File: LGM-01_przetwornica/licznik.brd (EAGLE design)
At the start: 68 x 48 mm, 34 parts, among them IC1 NE555, J1 22-27-2041-04, Q1 BC557, Q2 BC557, Q3 BC557, Q4 BC557, Q5 BC557, Q6 BC557, Q7 IRF840, T1 BC547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

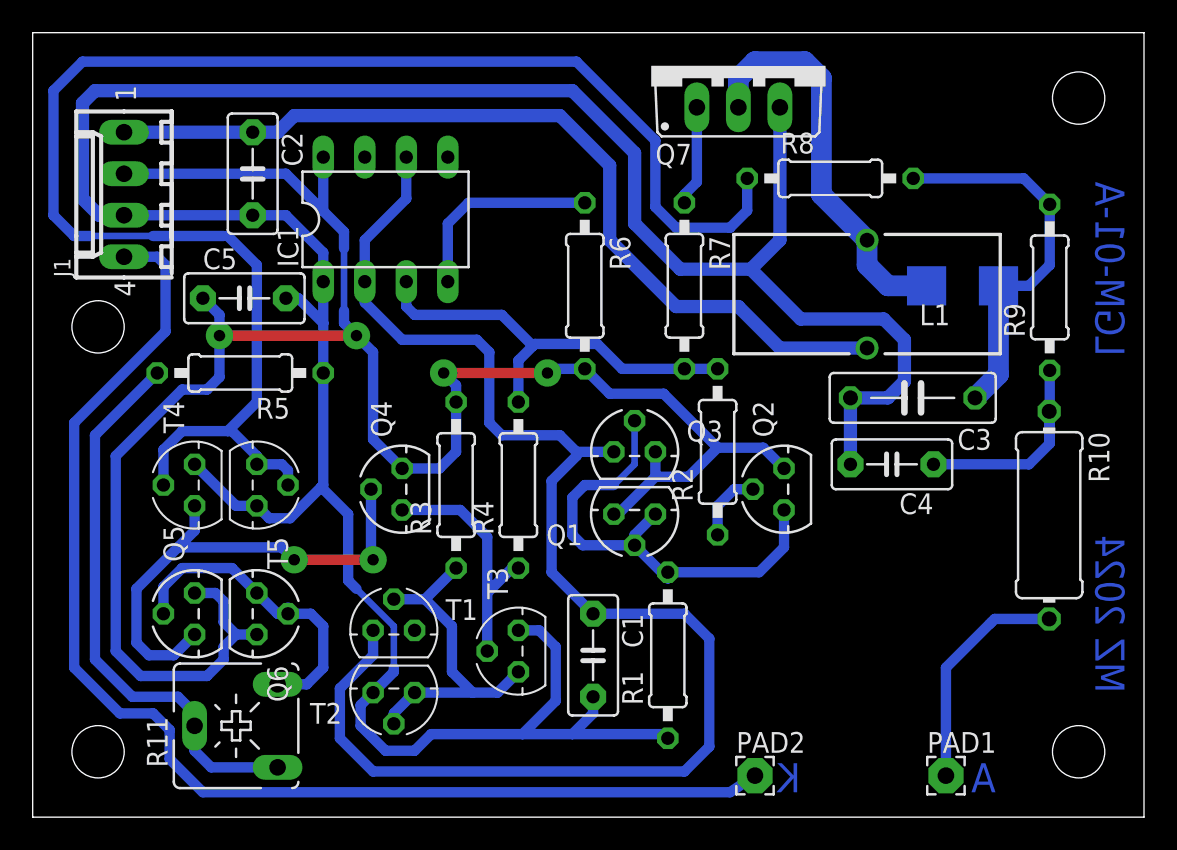
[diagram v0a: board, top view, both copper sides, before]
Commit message: Geiger SMPS cleanup
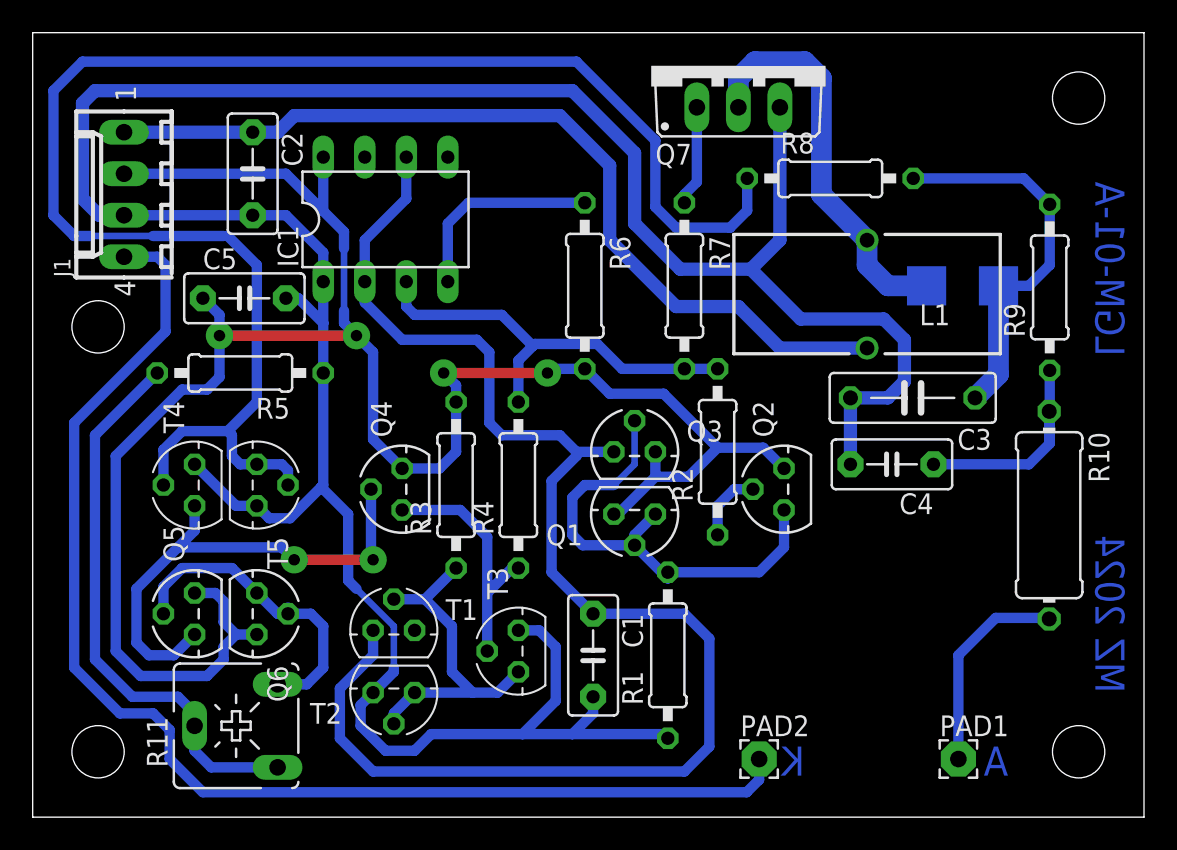
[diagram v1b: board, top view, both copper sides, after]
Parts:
- moved PAD1 1.27 mm to (56.6, 3.56)
- moved PAD2 1.05 mm to (44.5, 3.56)
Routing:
- net N$26: track 75.9 -> 77.4 mm
- net N$25: track 14.2 -> 12.9 mm
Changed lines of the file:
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@@
 <text x="65.024" y="28.194" size="1.778" layer="16" font="vector" ratio="15" rot="MR90">LGM-01-A</text>
 <text x="66.802" y="17.272" size="1.778" layer="16" font="vector" ratio="15" rot="MR270">MZ 2024</text>
-<text x="46.99" y="1.524" size="1.778" layer="16" font="vector" ratio="20" rot="MR0">K</text>
-<text x="58.928" y="1.524" size="1.778" layer="16" font="vector" ratio="20" rot="MR0">A</text>
+<text x="47.244" y="2.54" size="1.778" layer="16" font="vector" ratio="20" rot="MR0">K</text>
+<text x="59.69" y="2.54" size="1.778" layer="16" font="vector" ratio="20" rot="MR0">A</text>
 </plain>
 <attributes>
@@
 <element name="R4" library="resistor" package="0207/10" value="10k" x="29.718" y="20.32" rot="R90"/>
 <element name="R5" library="resistor" package="0207/10" value="33k" x="12.7" y="27.178" rot="R180"/>
-<element name="PAD1" library="wirepad" package="2,15/1,0" value="ANODA" x="55.88" y="2.54"/>
-<element name="PAD2" library="wirepad" package="2,15/1,0" value="KATODA" x="44.196" y="2.54"/>
+<element name="PAD1" library="wirepad" package="2,15/1,0" value="ANODA" x="56.642" y="3.556"/>
+<element name="PAD2" library="wirepad" package="2,15/1,0" value="KATODA" x="44.45" y="3.556"/>
 <element name="J1" library="con-molex" package="6410-04" value="22-27-2041-04" x="5.588" y="38.1" rot="R90">
 <attribute name="MF" value="" x="5.588" y="38.1" size="1.778" layer="27" rot="R90" display="off"/>
@@
 <wire x1="13.716" y1="25.4" x2="13.716" y2="33.782" width="0.635" layer="16"/>
 <wire x1="13.716" y1="33.782" x2="11.938" y2="35.56" width="0.635" layer="16"/>
-<wire x1="11.938" y1="23.622" x2="12.192" y2="23.622" width="0.635" layer="16"/>
-<wire x1="13.716" y1="22.098" x2="13.716" y2="21.59" width="0.635" layer="16"/>
 <wire x1="11.938" y1="35.56" x2="11.684" y2="35.56" width="0.4064" layer="16"/>
 <wire x1="7.366" y1="35.56" x2="3.556" y2="35.56" width="0.4064" layer="16"/>
@@
 <wire x1="15.621" y1="21.209" x2="15.24" y2="21.59" width="0.635" layer="16"/>
 <wire x1="15.24" y1="21.59" x2="13.716" y2="21.59" width="0.635" layer="16"/>
-<wire x1="12.192" y1="23.622" x2="13.716" y2="22.098" width="0.635" layer="16"/>
+<wire x1="13.716" y1="21.59" x2="12.7" y2="21.59" width="0.635" layer="16"/>
+<wire x1="12.7" y1="21.59" x2="12.192" y2="22.098" width="0.635" layer="16"/>
+<wire x1="12.192" y1="22.098" x2="12.192" y2="23.368" width="0.635" layer="16"/>
+<wire x1="12.192" y1="23.368" x2="11.938" y2="23.622" width="0.635" layer="16"/>
 </signal>
 <signal name="+5V">
@@
 <contactref element="R10" pad="2"/>
 <contactref element="PAD1" pad="1"/>
-<wire x1="55.88" y1="2.54" x2="55.88" y2="9.144" width="0.635" layer="16"/>
-<wire x1="55.88" y1="9.144" x2="58.547" y2="11.811" width="0.635" layer="16"/>
-<wire x1="58.547" y1="11.811" x2="58.674" y2="11.938" width="0.635" layer="16"/>
-<wire x1="62.198" y1="12.128" x2="58.864" y2="12.128" width="0.635" layer="16"/>
-<wire x1="58.864" y1="12.128" x2="58.674" y2="11.938" width="0.635" layer="16"/>
+<wire x1="56.642" y1="3.556" x2="56.642" y2="9.906" width="0.635" layer="16"/>
+<wire x1="56.642" y1="9.906" x2="58.928" y2="12.192" width="0.635" layer="16"/>
+<wire x1="58.928" y1="12.192" x2="62.134" y2="12.192" width="0.635" layer="16"/>
+<wire x1="62.134" y1="12.192" x2="62.198" y2="12.128" width="0.635" layer="16"/>
 </signal>
 <signal name="N$26">
 <contactref element="J1" pad="4"/>
 <contactref element="PAD2" pad="1"/>
-<wire x1="44.196" y1="2.54" x2="42.672" y2="1.524" width="0.635" layer="16"/>
-<wire x1="10.414" y1="1.524" x2="42.672" y2="1.524" width="0.635" layer="16"/>
+<wire x1="10.414" y1="1.524" x2="43.688" y2="1.524" width="0.635" layer="16"/>
 <wire x1="10.414" y1="1.524" x2="8.382" y2="3.556" width="0.635" layer="16"/>
 <wire x1="8.382" y1="3.556" x2="8.382" y2="5.334" width="0.635" layer="16"/>
@@
 <wire x1="8.128" y1="33.782" x2="7.62" y2="34.29" width="0.635" layer="16"/>
 <wire x1="7.62" y1="34.29" x2="5.588" y2="34.29" width="0.635" layer="16"/>
+<wire x1="43.688" y1="1.524" x2="44.45" y2="2.286" width="0.635" layer="16"/>
+<wire x1="44.45" y1="2.286" x2="44.45" y2="3.556" width="0.635" layer="16"/>
 </signal>
 <signal name="N$14">

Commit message: Added auxilary board
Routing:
- net N$12: track 97.3 -> 96.1 mm
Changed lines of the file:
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@@
 <layer number="19" name="Unrouted" color="6" fill="1" visible="yes" active="yes"/>
 <layer number="20" name="Dimension" color="15" fill="1" visible="yes" active="yes"/>
-<layer number="21" name="tPlace" color="7" fill="1" visible="no" active="yes"/>
+<layer number="21" name="tPlace" color="7" fill="1" visible="yes" active="yes"/>
 <layer number="22" name="bPlace" color="7" fill="1" visible="no" active="yes"/>
 <layer number="23" name="tOrigins" color="15" fill="1" visible="yes" active="yes"/>
 <layer number="24" name="bOrigins" color="15" fill="1" visible="yes" active="yes"/>
-<layer number="25" name="tNames" color="7" fill="1" visible="no" active="yes"/>
+<layer number="25" name="tNames" color="7" fill="1" visible="yes" active="yes"/>
 <layer number="26" name="bNames" color="7" fill="1" visible="no" active="yes"/>
 <layer number="27" name="tValues" color="7" fill="1" visible="no" active="yes"/>
@@
 <layer number="48" name="Document" color="7" fill="1" visible="yes" active="yes"/>
 <layer number="49" name="Reference" color="7" fill="1" visible="no" active="yes"/>
-<layer number="51" name="tDocu" color="7" fill="1" visible="no" active="yes"/>
+<layer number="51" name="tDocu" color="7" fill="1" visible="yes" active="yes"/>
 <layer number="52" name="bDocu" color="7" fill="1" visible="no" active="yes"/>
 <layer number="90" name="Modules" color="5" fill="1" visible="no" active="no"/>
@@
 <dimension x1="0" y1="48" x2="0" y2="0" x3="-17.018" y3="24" textsize="1.778" layer="48"/>
 <text x="65.024" y="28.194" size="1.778" layer="16" font="vector" ratio="15" rot="MR90">LGM-01-A</text>
-<text x="66.802" y="17.272" size="1.778" layer="16" font="vector" ratio="15" rot="MR270">MZ 2024</text>
+<text x="66.802" y="19.558" size="1.778" layer="16" font="vector" ratio="15" rot="MR270">MZ 2024</text>
 <text x="47.244" y="2.54" size="1.778" layer="16" font="vector" ratio="20" rot="MR0">K</text>
 <text x="59.69" y="2.54" size="1.778" layer="16" font="vector" ratio="20" rot="MR0">A</text>
@@
 <wire x1="11.938" y1="35.56" x2="11.684" y2="35.56" width="0.4064" layer="16"/>
 <wire x1="7.366" y1="35.56" x2="3.556" y2="35.56" width="0.4064" layer="16"/>
-<wire x1="2.54" y1="35.56" x2="3.556" y2="35.56" width="0.635" layer="16"/>
+<wire x1="3.048" y1="35.56" x2="3.556" y2="35.56" width="0.635" layer="16"/>
 <wire x1="11.684" y1="35.56" x2="7.366" y2="35.56" width="0.635" layer="16"/>
-<wire x1="2.54" y1="35.56" x2="1.27" y2="36.83" width="0.635" layer="16"/>
-<wire x1="1.27" y1="36.83" x2="1.27" y2="44.45" width="0.635" layer="16"/>
-<wire x1="1.27" y1="44.45" x2="3.048" y2="46.228" width="0.635" layer="16"/>
-<wire x1="3.048" y1="46.228" x2="33.274" y2="46.228" width="0.635" layer="16"/>
-<wire x1="33.274" y1="46.228" x2="38.1" y2="41.402" width="0.635" layer="16"/>
+<wire x1="3.048" y1="35.56" x2="1.778" y2="36.83" width="0.635" layer="16"/>
+<wire x1="1.778" y1="36.83" x2="1.778" y2="44.45" width="0.635" layer="16"/>
+<wire x1="1.778" y1="44.45" x2="3.302" y2="45.974" width="0.635" layer="16"/>
+<wire x1="3.302" y1="45.974" x2="33.528" y2="45.974" width="0.635" layer="16"/>
+<wire x1="33.528" y1="45.974" x2="38.1" y2="41.402" width="0.635" layer="16"/>
 <wire x1="38.1" y1="41.402" x2="38.1" y2="37.338" width="0.635" layer="16"/>
 <wire x1="38.1" y1="37.338" x2="39.37" y2="36.068" width="0.635" layer="16"/>

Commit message: Backup
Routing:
- net +5V: track 125.1 -> 124.4 mm
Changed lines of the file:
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@@
 <contactref element="R7" pad="1"/>
 <contactref element="Q7" pad="G"/>
-<wire x1="39.878" y1="37.592" x2="39.878" y2="38.1" width="0.635" layer="16"/>
-<wire x1="39.878" y1="38.1" x2="40.64" y2="38.862" width="0.635" layer="16"/>
-<wire x1="40.64" y1="38.862" x2="40.64" y2="43.434" width="0.635" layer="16"/>
+<wire x1="39.878" y1="37.592" x2="39.878" y2="38.862" width="0.635" layer="16"/>
+<wire x1="39.878" y1="38.862" x2="40.64" y2="39.624" width="0.635" layer="16"/>
+<wire x1="40.64" y1="39.624" x2="40.64" y2="43.434" width="0.635" layer="16"/>
 </signal>
 <signal name="N$12">
@@
 <wire x1="8.001" y1="20.32" x2="8.001" y2="22.479" width="0.635" layer="16"/>
 <wire x1="8.001" y1="22.479" x2="9.144" y2="23.622" width="0.635" layer="16"/>
-<wire x1="9.144" y1="23.622" x2="11.938" y2="23.622" width="0.635" layer="16"/>
-<wire x1="11.938" y1="23.622" x2="13.716" y2="25.4" width="0.635" layer="16"/>
 <wire x1="13.716" y1="25.4" x2="13.716" y2="33.782" width="0.635" layer="16"/>
 <wire x1="13.716" y1="33.782" x2="11.938" y2="35.56" width="0.635" layer="16"/>
@@
 <wire x1="13.716" y1="21.59" x2="12.7" y2="21.59" width="0.635" layer="16"/>
 <wire x1="12.7" y1="21.59" x2="12.192" y2="22.098" width="0.635" layer="16"/>
-<wire x1="12.192" y1="22.098" x2="12.192" y2="23.368" width="0.635" layer="16"/>
-<wire x1="12.192" y1="23.368" x2="11.938" y2="23.622" width="0.635" layer="16"/>
+<wire x1="9.144" y1="23.622" x2="11.938" y2="23.622" width="0.6096" layer="16"/>
+<wire x1="11.938" y1="23.622" x2="13.716" y2="25.4" width="0.6096" layer="16"/>
+<wire x1="12.192" y1="22.098" x2="11.938" y2="22.352" width="0.6096" layer="16"/>
+<wire x1="11.938" y1="22.352" x2="11.938" y2="23.622" width="0.6096" layer="16"/>
 </signal>
 <signal name="+5V">
@@
 <wire x1="20.828" y1="23.114" x2="20.828" y2="28.448" width="0.635" layer="16"/>
 <wire x1="20.828" y1="28.448" x2="19.812" y2="29.464" width="0.635" layer="16"/>
-<via x="11.43" y="29.464" extent="1-16" drill="0.7" diameter="1.6764"/>
+<via x="10.414" y="29.464" extent="1-16" drill="0.7" diameter="1.6764"/>
 <via x="19.812" y="29.464" extent="1-16" drill="0.7" diameter="1.6764"/>
-<wire x1="11.43" y1="29.464" x2="19.812" y2="29.464" width="0.635" layer="1"/>
-<wire x1="11.43" y1="29.464" x2="11.43" y2="26.924" width="0.635" layer="16"/>
-<wire x1="11.43" y1="26.924" x2="10.668" y2="26.162" width="0.635" layer="16"/>
-<wire x1="10.668" y1="26.162" x2="9.144" y2="26.162" width="0.635" layer="16"/>
-<wire x1="9.144" y1="26.162" x2="5.08" y2="22.098" width="0.635" layer="16"/>
+<wire x1="10.414" y1="29.464" x2="19.812" y2="29.464" width="0.635" layer="1"/>
+<wire x1="10.414" y1="29.464" x2="10.414" y2="27.432" width="0.635" layer="16"/>
+<wire x1="10.414" y1="27.432" x2="5.08" y2="22.098" width="0.635" layer="16"/>
 <wire x1="31.75" y1="27.432" x2="33.782" y2="27.432" width="0.635" layer="16"/>
 <wire x1="33.782" y1="27.432" x2="35.306" y2="25.908" width="0.635" layer="16"/>
 <wire x1="35.306" y1="25.908" x2="38.608" y2="25.908" width="0.635" layer="16"/>
 <contactref element="C5" pad="1"/>
-<wire x1="11.43" y1="29.464" x2="11.43" y2="30.734" width="0.635" layer="16"/>
-<wire x1="11.43" y1="30.734" x2="10.414" y2="31.75" width="0.635" layer="16"/>
+<wire x1="10.414" y1="29.464" x2="10.414" y2="31.75" width="0.635" layer="16"/>
 <wire x1="12.446" y1="11.176" x2="11.684" y2="10.414" width="0.635" layer="16"/>
 <wire x1="11.684" y1="10.414" x2="11.684" y2="9.652" width="0.635" layer="16"/>
@@
 <wire x1="3.81" y1="23.368" x2="7.62" y2="27.178" width="0.635" layer="16"/>
 </signal>
+<signal name="N$15">
+</signal>
 </signals>
